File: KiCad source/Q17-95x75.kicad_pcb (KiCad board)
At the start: 2 copper layers, 96.5 x 76.2 mm, 84 parts, among them J1 TerminalBlock, Q1 IRF610, Q10 2SA970, Q11 BS250, Q12 2SC2240 / AC181, Q13 IRF610, Q14 IRF9610, Q15 FQA46N15, Q16 FQA36P15, Q2 2SA970, Q3 2SC2240, Q4 IRF9610, Q5 IRF9610, Q6 IRF610, Q7 2SC2240, Q8 2N7000, Q9 BS250, U1 DIP-8_W7.62mm_Socket, U1 OPA1641

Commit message: PCB Q17-95x75 version 10b6
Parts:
- moved Q9 8.26 mm to (128.0, 54.5), turned to 90 degrees
- moved Q11 6.48 mm to (134.9, 54.5), turned to 90 degrees
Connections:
- Q11 pad 1: Net-(R24-Pad1) -> Net-(Q10-Pad2)
- Q11 pad 3: Net-(Q10-Pad2) -> Net-(R24-Pad1)
- Q9 pad 1: Net-(Q8-Pad3) -> Net-(R3-Pad2)
- Q9 pad 3: Net-(R3-Pad2) -> Net-(Q8-Pad3)
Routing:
- net Net-(Q10-Pad2): track 17.8 -> 8.53 mm
- net Net-(R3-Pad2): track 9.90 -> 17.8 mm
- net Net-(Q8-Pad3): track 45.4 -> 39.2 mm
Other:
- board text added: "Q17 1.0b6"
- board text removed: "Q17 1.0b5"

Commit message: Update Q17-95x75.kicad_pcb
1.0b6
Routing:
- net Net-(L1-Pad2): track 119.8 -> 124.9 mm
- net Net-(C17-Pad1): track 15.7 -> 17.1 mm
- net GNDPWR: track 152.9 -> 152.0 mm
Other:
- board text added: "Q17 1.0b7"
- board text removed: "Q17 1.0b6"

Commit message: PCB version 1.0b8
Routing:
- net GNDPWR: track 152.0 -> 190.1 mm
- net Net-(L1-Pad2): track 124.9 -> 127.5 mm
- net Net-(C17-Pad1): track 17.1 -> 18.9 mm
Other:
- board text added: "Q17 1.0b8"
- board text added: "QUAD405 Audiophile Tiberiu Vicol PCB Design by Stef"
- board text removed: "Q17 1.0b7"
- board text removed: "QUAD405 Audiophile by Tiberiu Vicol PCB Design by Stef"

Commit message: PCB version 1.0b9
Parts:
- moved Faston Connector 0.71 mm to (153.7, 109.1)
- moved Faston Connector 0.71 mm to (153.7, 68.5)
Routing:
- net Net-(C16-Pad2): track 88.0 -> 89.5 mm
- net Net-(C15-Pad1): track 69.9 -> 70.6 mm
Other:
- board text added: "Q17 1.0b9"
- board text removed: "Q17 1.0b8"
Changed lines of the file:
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@@
     (title "QUAD405 Reborn")
     (date "2021-11-13")
-    (rev "1.0b8")
+    (rev "1.0b9")
     (company "PCB design by Stef")
     (comment 1 "Zize 95 x 75 mm")
@@
   )
   (footprint "Connector_Faston:Faston_connector" (layer "F.Cu")
-    (at 154.376441 109.1438 180)
+    (at 153.67 109.1438 180)
     (attr through_hole)
     (fp_text reference "Faston Connector" (at -5.715 2.54) (layer "F.Fab")
@@
   )
   (footprint "Connector_Faston:Faston_connector" (layer "F.Cu")
-    (at 154.376441 68.5038 180)
+    (at 153.67 68.5038 180)
     (attr through_hole)
     (fp_text reference "Faston Connector" (at -2.54 2.54) (layer "F.Fab")
@@
     (effects (font (size 0.5 0.5) (thickness 0.125)))
   )
-  (gr_text "Q17 1.0b8" (at 145.288 109.728) (layer "F.SilkS")
+  (gr_text "Q17 1.0b9" (at 145.288 109.728) (layer "F.SilkS")
     (effects (font (size 1 1) (thickness 0.25)))
   )
@@
   (segment (start 139.274711 108.629289) (end 131.489289 108.629289) (width 0.5) (layer "F.Cu") (net 8))
   (via (at 141.224 106.68) (size 0.8) (drill 0.4) (layers "F.Cu" "B.Cu") (free) (net 8))
-  (segment (start 153.070241 106.68) (end 155.686441 104.0638) (width 0.5) (layer "B.Cu") (net 8))
-  (segment (start 141.224 106.68) (end 153.070241 106.68) (width 0.5) (layer "B.Cu") (net 8))
+  (segment (start 141.859 106.045) (end 153.705241 106.045) (width 0.5) (layer "B.Cu") (net 8))
+  (segment (start 141.224 106.68) (end 141.859 106.045) (width 0.5) (layer "B.Cu") (net 8))
+  (segment (start 153.705241 106.045) (end 155.686441 104.0638) (width 0.5) (layer "B.Cu") (net 8))
   (segment (start 111.871441 59.6138) (end 111.196441 60.2888) (width 0.5) (layer "F.Cu") (net 9))
   (segment (start 119.451441 51.9938) (end 127.071441 59.6138) (width 0.5) (layer "F.Cu") (net 9))
@@
   (segment (start 162.3822 68.5038) (end 162.9918 68.5038) (width 0.25) (layer "F.Cu") (net 17))
   (segment (start 178.506441 78.6638) (end 178.506441 78.0288) (width 1.5) (layer "F.Cu") (net 17))
-  (segment (start 154.376441 68.5038) (end 159.456441 68.5038) (width 1.8) (layer "F.Cu") (net 17))
   (segment (start 170.434 68.595559) (end 170.434 65.814139) (width 1.8) (layer "F.Cu") (net 17))
+  (segment (start 153.67 68.5038) (end 162.9918 68.5038) (width 1.8) (layer "F.Cu") (net 17))
   (segment (start 173.466441 71.628) (end 170.434 68.595559) (width 1.8) (layer "F.Cu") (net 17))
   (segment (start 173.902327 81.2038) (end 174.1704 81.2038) (width 1) (layer "F.Cu") (net 17))
@@
   (segment (start 166.2554 99.92158) (end 166.2554 98.534841) (width 1) (layer "F.Cu") (net 17))
   (segment (start 172.17088 82.935247) (end 173.902327 81.2038) (width 1) (layer "F.Cu") (net 17))
-  (segment (start 162.9918 68.5038) (end 159.456441 68.5038) (width 1.8) (layer "F.Cu") (net 17))
   (segment (start 183.7904 78.6638) (end 185.0604 77.3938) (width 1.5) (layer "F.Cu") (net 17))
   (segment (start 162.3822 68.5038) (end 163.1442 68.5038) (width 1.8) (layer "F.Cu") (net 17))
   (segment (start 172.17088 92.619361) (end 172.17088 82.935247) (width 1) (layer "F.Cu") (net 17))
-  (segment (start 166.2554 76.1238) (end 166.2554 82.6646) (width 1) (layer "F.Cu") (net 18))
+  (segment (start 158.186441 102.7938) (end 164.455889 96.524352) (width 1) (layer "F.Cu") (net 18))
   (segment (start 177.236441 96.4438) (end 177.236441 95.1738) (width 1.8) (layer "F.Cu") (net 18))
-  (segment (start 164.455889 84.464111) (end 164.455889 86.696963) (width 1) (layer "F.Cu") (net 18))
-  (segment (start 166.2554 82.6646) (end 164.455889 84.464111) (width 1) (layer "F.Cu") (net 18))
-  (segment (start 158.186441 102.7938) (end 158.186441 105.3338) (width 1) (layer "F.Cu") (net 18))
+  (segment (start 158.75 109.1438) (end 161.07778 111.47158) (width 2) (layer "F.Cu") (net 18))
+  (segment (start 161.07778 111.47158) (end 168.981441 111.47158) (width 2) (layer "F.Cu") (net 18))
+  (segment (start 164.465 86.706074) (end 164.455889 86.696963) (width 1) (layer "F.Cu") (net 18))
+  (segment (start 166.2554 82.6646) (end 166.2554 76.1238) (width 1) (layer "F.Cu") (net 18))
+  (segment (start 164.455889 96.524352) (end 164.455889 89.016197) (width 1) (layer "F.Cu") (net 18))
   (segment (start 168.981441 111.47158) (end 171.058661 111.47158) (width 2) (layer "F.Cu") (net 18))
   (segment (start 174.696441 93.9038) (end 174.1704 93.9038) (width 0.25) (layer "F.Cu") (net 18))
-  (segment (start 154.376441 109.1438) (end 159.456441 109.1438) (width 2) (layer "F.Cu") (net 18))
-  (segment (start 164.465 89.007086) (end 164.455889 89.016197) (width 1) (layer "F.Cu") (net 18))
+  (segment (start 153.67 109.22) (end 154.300241 109.22) (width 1) (layer "F.Cu") (net 18))
+  (segment (start 153.7462 109.1438) (end 158.75 109.1438) (width 2) (layer "F.Cu") (net 18))
   (segment (start 177.236441 96.4438) (end 183.1554 96.4438) (width 2) (layer "F.Cu") (net 18))
   (segment (start 177.236441 95.1738) (end 175.966441 93.9038) (width 1.8) (layer "F.Cu") (net 18))
   (segment (start 166.2554 76.1238) (end 166.2554 75.79158) (width 0.25) (layer "F.Cu") (net 18))
-  (segment (start 161.784221 111.47158) (end 168.981441 111.47158) (width 2) (layer "F.Cu") (net 18))
-  (segment (start 164.455889 86.696963) (end 164.465 86.706074) (width 1) (layer "F.Cu") (net 18))
-  (segment (start 164.455889 89.016197) (end 164.455889 96.524352) (width 1) (layer "F.Cu") (net 18))
+  (segment (start 158.186441 105.3338) (end 158.186441 102.7938) (width 1) (layer "F.Cu") (net 18))
+  (segment (start 153.67 109.22) (end 153.7462 109.1438) (width 2) (layer "F.Cu") (net 18))
+  (segment (start 164.455889 84.464111) (end 166.2554 82.6646) (width 1) (layer "F.Cu") (net 18))
   (segment (start 178.466441 104.0638) (end 177.236441 102.8338) (width 2) (layer "F.Cu") (net 18))
-  (segment (start 164.455889 96.524352) (end 158.186441 102.7938) (width 1) (layer "F.Cu") (net 18))
-  (segment (start 159.456441 109.1438) (end 161.784221 111.47158) (width 2) (layer "F.Cu") (net 18))
+  (segment (start 164.455889 89.016197) (end 164.465 89.007086) (width 1) (layer "F.Cu") (net 18))
   (segment (start 175.966441 93.9038) (end 174.696441 93.9038) (width 1.8) (layer "F.Cu") (net 18))
   (segment (start 183.1554 96.4438) (end 185.0604 98.3488) (width 2) (layer "F.Cu") (net 18))
-  (segment (start 164.465 86.706074) (end 164.465 89.007086) (width 1) (layer "F.Cu") (net 18))
-  (segment (start 158.186441 105.3338) (end 154.376441 109.1438) (width 1) (layer "F.Cu") (net 18))
   (segment (start 177.236441 102.8338) (end 177.236441 96.4438) (width 2) (layer "F.Cu") (net 18))
   (segment (start 171.058661 111.47158) (end 178.466441 104.0638) (width 2) (layer "F.Cu") (net 18))
+  (segment (start 164.455889 86.696963) (end 164.455889 84.464111) (width 1) (layer "F.Cu") (net 18))
+  (segment (start 164.465 89.007086) (end 164.465 86.706074) (width 1) (layer "F.Cu") (net 18))
+  (segment (start 154.300241 109.22) (end 158.186441 105.3338) (width 1) (layer "F.Cu") (net 18))
   (segment (start 142.875 84.450241) (end 146.756441 80.5688) (width 1) (layer "F.Cu") (net 19))
   (segment (start 142.875 90.777359) (end 142.875 84.450241) (width 1) (layer "F.Cu") (net 19))

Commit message: PCB version 1.0b10
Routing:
- net GND: track 225.0 -> 225.6 mm
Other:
- board text added: "Q17 1.0b10"
- board text removed: "Q17 1.0b9"
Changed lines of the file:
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@@
     (title "QUAD405 Reborn")
     (date "2021-11-13")
-    (rev "1.0b9")
+    (rev "1.0b10")
     (company "PCB design by Stef")
     (comment 1 "Zize 95 x 75 mm")
@@
     (effects (font (size 0.5 0.5) (thickness 0.125)))
   )
-  (gr_text "Q17 1.0b9" (at 145.288 109.728) (layer "F.SilkS")
+  (gr_text "Q17 1.0b10" (at 145.288 109.728) (layer "F.SilkS")
     (effects (font (size 1 1) (thickness 0.25)))
   )
@@
   (segment (start 120.904 121.661241) (end 120.240952 122.324289) (width 1) (layer "B.Cu") (net 1))
   (segment (start 124.407419 59.6138) (end 127.658619 62.865) (width 1) (layer "B.Cu") (net 1))
-  (segment (start 156.916441 107.8338) (end 160.686441 104.0638) (width 1) (layer "B.Cu") (net 1))
   (segment (start 101.671441 104.0638) (end 103.484118 105.876477) (width 1) (layer "B.Cu") (net 1))
   (segment (start 130.294263 62.865) (end 132.910463 60.2488) (width 1) (layer "B.Cu") (net 1))
-  (segment (start 157.551441 114.8588) (end 156.916441 114.2238) (width 1) (layer "B.Cu") (net 1))
   (segment (start 107.386441 57.7088) (end 107.386441 61.4788) (width 1) (layer "B.Cu") (net 1))
   (segment (start 99.044441 99.860261) (end 101.671441 102.487261) (width 1) (layer "B.Cu") (net 1))
@@
   (segment (start 107.386441 61.4788) (end 111.196441 65.2888) (width 1) (layer "B.Cu") (net 1))
   (segment (start 111.196441 65.2888) (end 109.22 67.265241) (width 1) (layer "B.Cu") (net 1))
+  (segment (start 156.21 108.540241) (end 160.686441 104.0638) (width 1) (layer "B.Cu") (net 1))
   (segment (start 104.085964 84.286477) (end 104.044441 84.328) (width 1) (layer "B.Cu") (net 1))
   (segment (start 144.78 124.46) (end 145.465961 123.774039) (width 1) (layer "B.Cu") (net 1))
@@
   (segment (start 112.466441 84.286477) (end 110.236 86.516918) (width 1) (layer "B.Cu") (net 1))
   (segment (start 145.465961 123.774039) (end 145.465961 121.22928) (width 1) (layer "B.Cu") (net 1))
+  (segment (start 157.551441 114.8588) (end 156.21 113.517359) (width 1) (layer "B.Cu") (net 1))
   (segment (start 148.026441 118.6688) (end 154.376441 118.6688) (width 1) (layer "B.Cu") (net 1))
-  (segment (start 156.916441 114.2238) (end 156.916441 107.8338) (width 1) (layer "B.Cu") (net 1))
   (segment (start 111.196441 65.2888) (end 113.061441 65.2888) (width 1) (layer "B.Cu") (net 1))
   (segment (start 132.910463 60.2488) (end 148.026441 60.2488) (width 1) (layer "B.Cu") (net 1))
@@
   (segment (start 99.044441 99.517281) (end 99.044441 99.860261) (width 0.25) (layer "B.Cu") (net 1))
   (segment (start 158.186441 114.8588) (end 157.551441 114.8588) (width 0.25) (layer "B.Cu") (net 1))
+  (segment (start 156.21 113.517359) (end 156.21 108.540241) (width 1) (layer "B.Cu") (net 1))
   (segment (start 127.658619 62.865) (end 130.294263 62.865) (width 1) (layer "B.Cu") (net 1))
   (segment (start 109.22 81.040036) (end 112.466441 84.286477) (width 1) (layer "B.Cu") (net 1))
@@
   (segment (start 157.354326 54.483) (end 149.982241 54.483) (width 1.2) (layer "B.Cu") (net 12))
   (segment (start 145.6436 52.5018) (end 144.1958 51.054) (width 1) (layer "B.Cu") (net 12))
-  (segment (start 153.67 58.9026) (end 155.0162 60.2488) (width 2.5) (layer "F.Cu") (net 13))
-  (segment (start 153.67 52.4835) (end 153.67 58.9026) (width 2.5) (layer "F.Cu") (net 13))
-  (segment (start 155.0162 60.2488) (end 158.186441 60.2488) (width 2.5) (layer "F.Cu") (net 13))
-  (via (at 153.67 52.4835) (size 1.8) (drill 0.9) (layers "F.Cu" "B.Cu") (free) (net 13))
-  (segment (start 178.292889 71.454448) (end 178.292889 53.515389) (width 0.9) (layer "B.Cu") (net 13))
+  (segment (start 153.669999 52.352791) (end 153.67 58.9026) (width 2.2) (layer "F.Cu") (net 13))
+  (segment (start 155.0162 60.2488) (end 158.186441 60.2488) (width 2.2) (layer "F.Cu") (net 13))
+  (segment (start 153.67 58.9026) (end 155.0162 60.2488) (width 2.2) (layer "F.Cu") (net 13))
+  (via (at 153.669999 52.352791) (size 2) (drill 1) (layers "F.Cu" "B.Cu") (free) (net 13))
   (segment (start 164.576441 104.0638) (end 167.751441 107.2388) (width 1) (layer "B.Cu") (net 13))
-  (segment (start 178.292889 53.515389) (end 175.5775 50.8) (width 0.9) (layer "B.Cu") (net 13))
-  (segment (start 155.3535 50.8) (end 153.67 52.4835) (width 0.9) (layer "B.Cu") (net 13))
+  (segment (start 155.22279 50.8) (end 153.669999 52.352791) (width 0.9) (layer "B.Cu") (net 13))
   (segment (start 159.8754 95.1738) (end 159.8754 99.362759) (width 1) (layer "B.Cu") (net 13))
   (segment (start 159.8754 95.1738) (end 157.48 92.7784) (width 1.8) (layer "B.Cu") (net 13))
@@
   (segment (start 137.866441 102.7938) (end 151.836441 102.7938) (width 1.8) (layer "B.Cu") (net 13))
   (segment (start 168.981441 118.97158) (end 167.531441 118.97158) (width 1) (layer "B.Cu") (net 13))
-  (segment (start 175.5775 50.8) (end 155.3535 50.8) (width 0.9) (layer "B.Cu") (net 13))
+  (segment (start 178.292889 71.454448) (end 178.292889 53.515389) (width 0.9) (layer "B.Cu") (net 13))
   (segment (start 157.48 82.5384) (end 154.8754 79.9338) (width 1.8) (layer "B.Cu") (net 13))
+  (segment (start 178.292889 53.515389) (end 175.5775 50.8) (width 0.9) (layer "B.Cu") (net 13))
   (segment (start 173.466441 104.9963) (end 173.466441 104.0638) (width 0.25) (layer "B.Cu") (net 13))
   (segment (start 157.48 92.7784) (end 157.48 82.5384) (width 1.8) (layer "B.Cu") (net 13))
@@
   (segment (start 137.866441 100.7688) (end 132.906441 95.8088) (width 1.8) (layer "B.Cu") (net 13))
   (segment (start 167.751441 107.2388) (end 171.223941 107.2388) (width 1) (layer "B.Cu") (net 13))
+  (segment (start 175.5775 50.8) (end 155.22279 50.8) (width 0.9) (layer "B.Cu") (net 13))
   (segment (start 137.866441 102.7938) (end 137.866441 100.7688) (width 1.8) (layer "B.Cu") (net 13))
   (segment (start 164.576441 61.26658) (end 168.981441 56.86158) (width 1.8) (layer "B.Cu") (net 13))

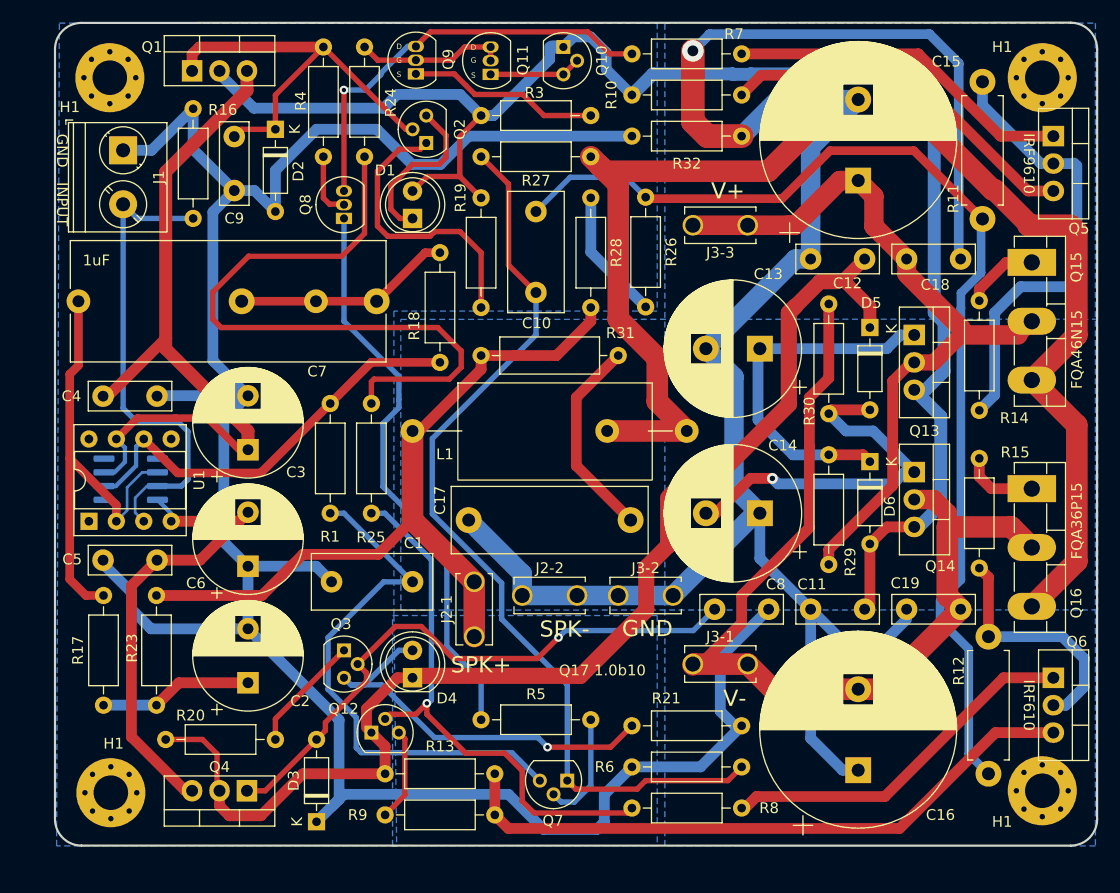
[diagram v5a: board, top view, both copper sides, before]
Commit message: PCB version 10b11
- Precision timing of the fixing holes compared to the original PCB.
- Displacement of R11 and R12.
- Fixed various overlaps.
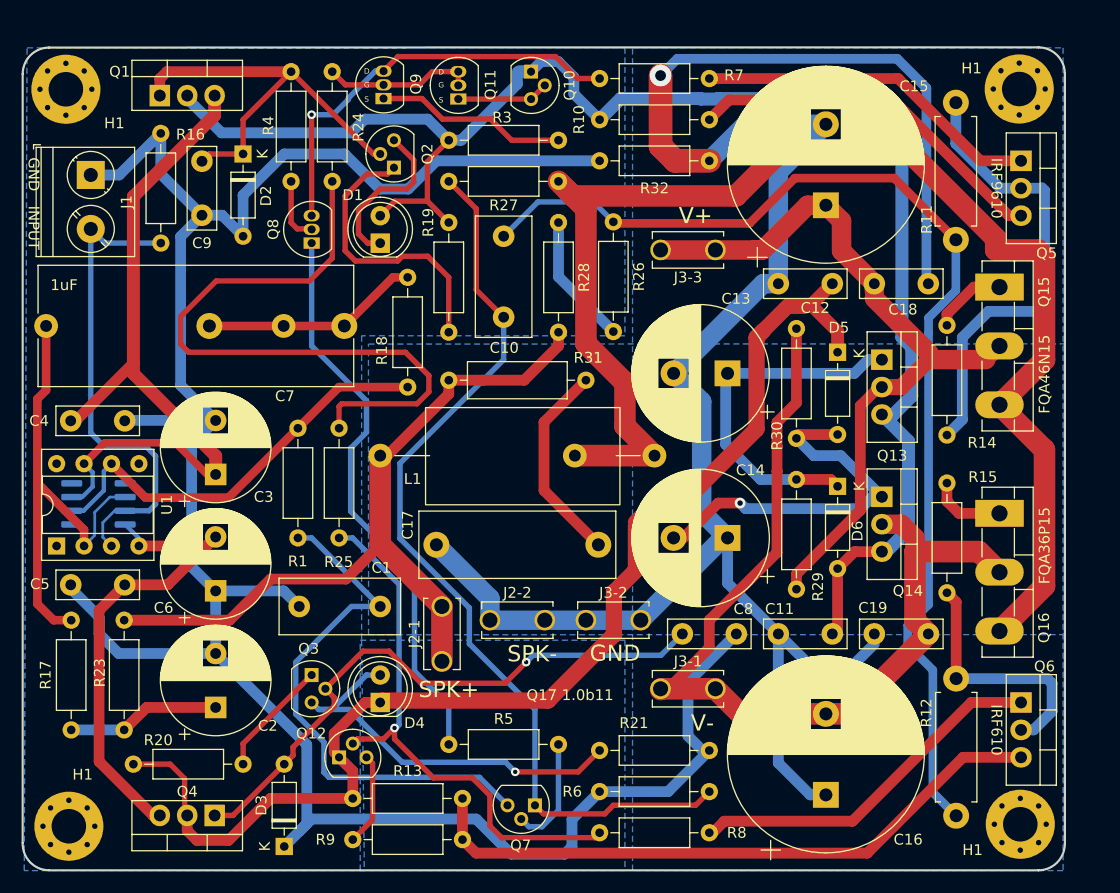
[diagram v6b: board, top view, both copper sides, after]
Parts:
- moved H1 4.98 mm to (95.9, 124.2)
- moved R12 4.90 mm to (178.1, 123.2)
- moved H1 4.21 mm to (95.6, 55.9)
- moved R27 3.77 mm to (131.1, 64.4)
- moved C13 3.77 mm to (156.9, 82.2)
- moved C14 3.77 mm to (156.9, 97.5)
- moved C17 3.77 mm to (144.9, 98.1)
- moved C18 3.77 mm to (175.5, 73.9)
- moved C19 3.77 mm to (175.5, 106.3)
- moved C8 3.77 mm to (157.7, 106.3)
- moved D5 3.77 mm to (167.1, 80.3)
- moved D6 3.77 mm to (167.1, 92.7)
- moved Faston Connector 3.77 mm to (134.9, 105.1)
- moved Q10 3.77 mm to (138.7, 54.3)
- moved Q13 3.77 mm to (171.2, 80.9)
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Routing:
- net Net-(C10-Pad1): track 103.6 -> 105.2 mm
- net Net-(Q6-Pad2): track 22.6 -> 23.5 mm
- net Net-(Q5-Pad2): track 42.6 -> 43.2 mm
- net Net-(L1-Pad2): track 127.5 -> 128.0 mm
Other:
- board text added: "Q17 1.0b11"
- board text removed: "Q17 1.0b10"

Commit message: Update PCB to 10b12
- Changed footprint for KSC1845 (Q2, Q7 and Q12).
- Updated transistors references on diagram and PCB.
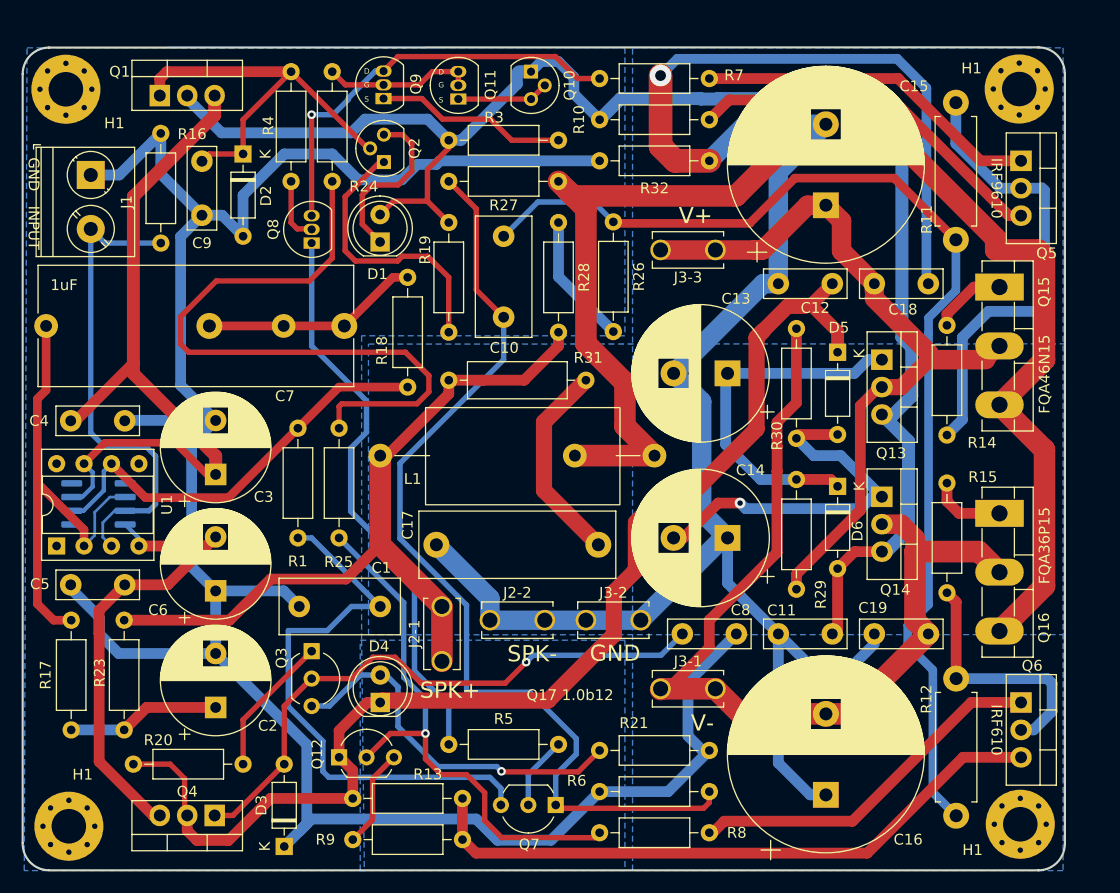
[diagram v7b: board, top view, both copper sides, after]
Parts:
- Q10, Q2: value 2SA970 -> KSA992
- Q11, Q9: value BS250 -> BS250P
- Q12: value 2SC2240 / AC181 -> KSC1845; footprint Package_TO_SOT_THT:TO-92 -> Package_TO_SOT_THT:TO-92_Inline_Wide
- Q3, Q7: value 2SC2240 -> KSC1845; footprint Package_TO_SOT_THT:TO-92 -> Package_TO_SOT_THT:TO-92_Inline_Wide
- moved Q3 2.21 mm to (118.4, 108.0)
- moved Q7 1.93 mm to (141.0, 122.2)
- moved Q2 1.06 mm to (125.1, 62.7)
- moved D1 0.11 mm to (124.7, 70.1)
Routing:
- net Net-(C10-Pad2): track 86.4 -> 90.4 mm
- net Net-(Q7-Pad2): track 10.5 -> 6.77 mm
- net GND: track 225.6 -> 222.3 mm
- net Net-(C1-Pad1): track 49.8 -> 52.7 mm
- net Net-(D4-Pad2): track 37.2 -> 34.5 mm
- net Net-(Q3-Pad1): track 10.9 -> 13.1 mm
- net Net-(C9-Pad2): track 39.0 -> 37.8 mm
- net Net-(Q2-Pad1): track 26.7 -> 26.0 mm
- net Net-(D1-Pad1): track 15.4 -> 16.0 mm
- net Net-(Q12-Pad3): track 8.61 -> 9.20 mm
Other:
- board text added: "Q17 1.0b12"
- board text removed: "Q17 1.0b11"
